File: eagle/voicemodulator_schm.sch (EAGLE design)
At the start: 39 parts, among them T1 2N5089, T2 2N5089, T3 2N5089, T4 2N5089

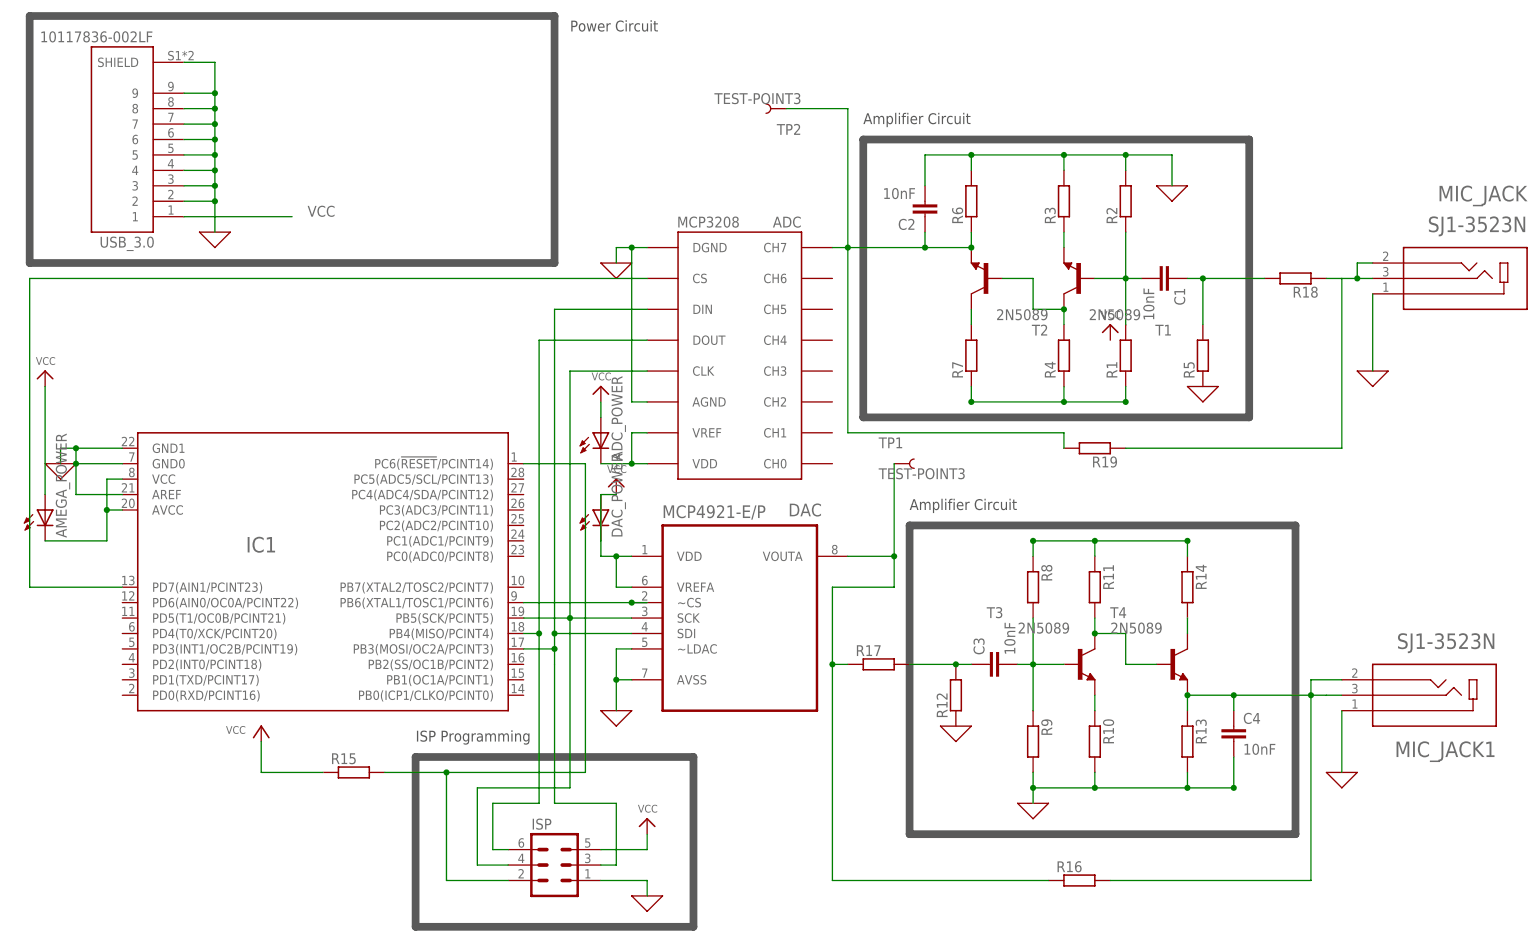
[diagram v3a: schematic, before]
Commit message: Grounded LEDs on power pins, added bypass caps at power pins
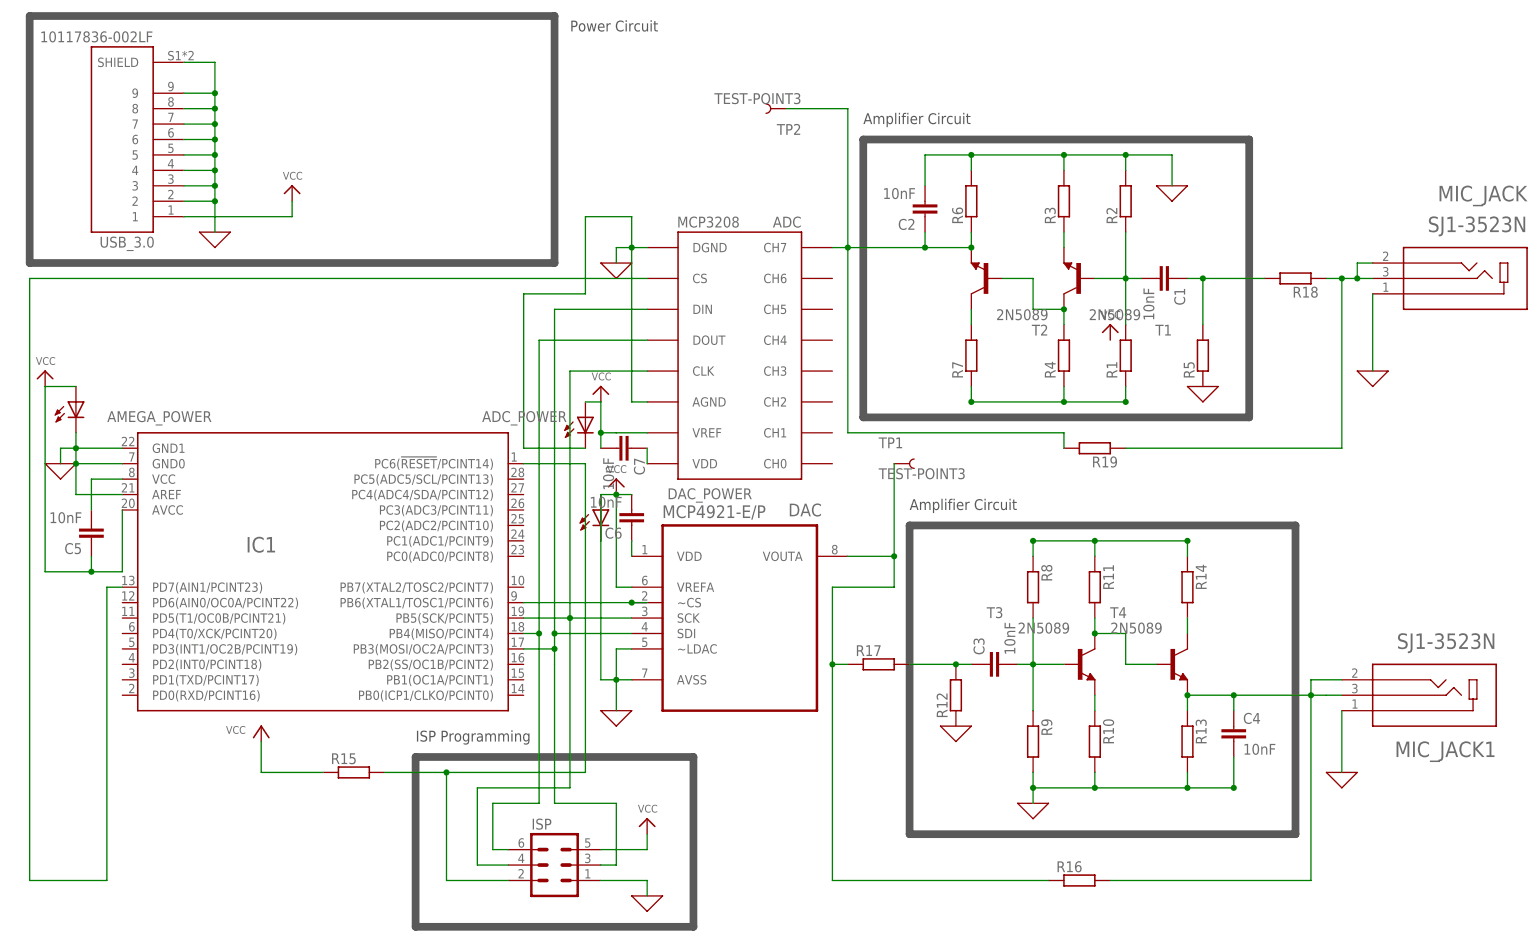
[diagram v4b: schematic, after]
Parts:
- added C5, C6, C7: 10nF, SparkFun-Capacitors:10NF-0603-50V-10%
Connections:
- removed net 0: ADC.AGND, ADC.DGND, C2.2, C4.2, DAC.AVSS, DAC.~LDAC, IC1.AREF, IC1.GND0, IC1.GND1, ISP.1, MIC_JACK.1, MIC_JACK1.1, R10.1, R12.2, R13.1, R2.1, R3.1, R5.2, R6.1, R9.1, USB_3.0.2, USB_3.0.3, USB_3.0.4, USB_3.0.5, USB_3.0.6, USB_3.0.7, USB_3.0.8, USB_3.0.9, USB_3.0.SHIELD
- new net GND: ADC.AGND, ADC.DGND, ADC_POWER.C, AMEGA_POWER.C, C2.2, C4.2, C6.2, DAC.AVSS, DAC.VREFA, DAC.~LDAC, DAC_POWER.A, DAC_POWER.C, IC1.AREF, IC1.GND0, IC1.GND1, ISP.1, MIC_JACK.1, MIC_JACK1.1, R10.1, R12.2, R13.1, R2.1, R3.1, R5.2, R6.1, R9.1, USB_3.0.2, USB_3.0.3, USB_3.0.4, USB_3.0.5, USB_3.0.6, USB_3.0.7, USB_3.0.8, USB_3.0.9, USB_3.0.SHIELD
- new net N$25: C5.2, IC1.VCC
- net N$18: now also C6.1, DAC.VDD; no longer ADC.VDD, ADC.VREF, ADC_POWER.C
- net N$21: now also ADC.VDD, C7.1; no longer AMEGA_POWER.C, IC1.AVCC, IC1.VCC
- net VCC: now also ADC.VREF, C5.1, C7.2, IC1.AVCC; no longer DAC.VDD, DAC.VREFA, DAC_POWER.A, DAC_POWER.C
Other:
- moved on the sheet: ADC_POWER, AMEGA_POWER

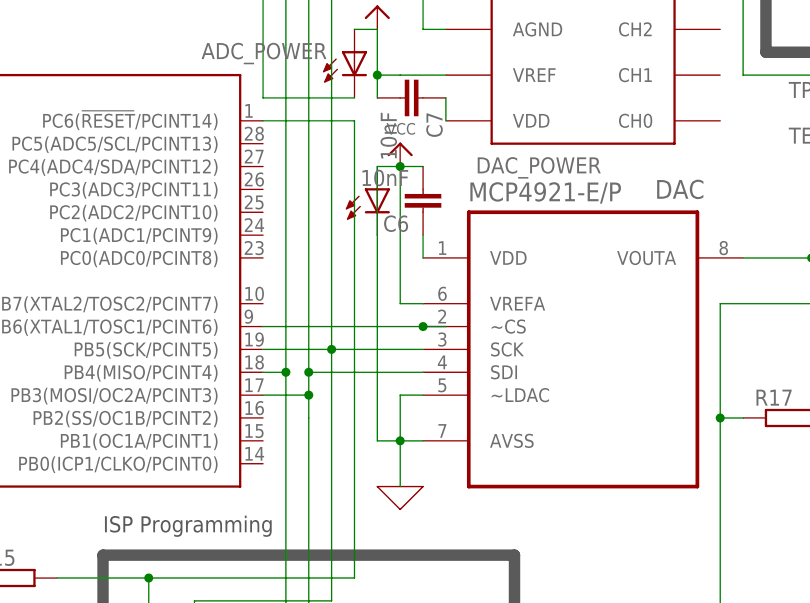
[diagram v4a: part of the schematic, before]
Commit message: Fixed erc error I missed on DAC
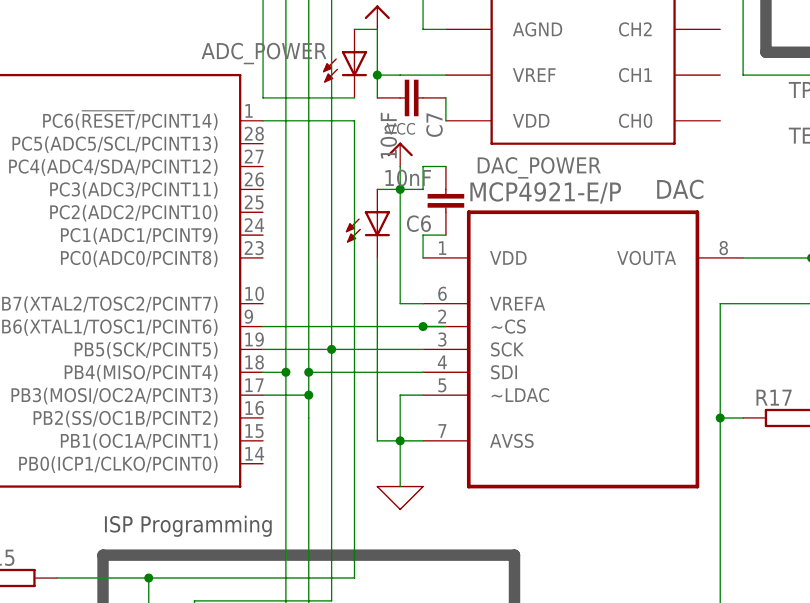
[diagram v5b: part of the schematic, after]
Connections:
- net GND: no longer C6.2, DAC.VREFA, DAC_POWER.A
- net VCC: now also C6.2, DAC.VREFA, DAC_POWER.A
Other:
- moved on the sheet: C6, DAC_POWER
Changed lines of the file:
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@@
 <attribute name="VALUE" x="48.895" y="46.228" size="1.778" layer="96" rot="R90"/>
 </instance>
-<instance part="DAC_POWER" gate="G$1" x="45.72" y="35.56">
+<instance part="DAC_POWER" gate="G$1" x="45.72" y="33.02">
 <attribute name="NAME" x="70.612" y="39.116" size="1.778" layer="95" rot="R180"/>
-<attribute name="VALUE" x="51.435" y="30.988" size="1.778" layer="96" rot="R90"/>
+<attribute name="VALUE" x="51.435" y="28.448" size="1.778" layer="96" rot="R90"/>
 </instance>
 <instance part="AMEGA_POWER" gate="G$1" x="-40.64" y="53.34">
@@
 <attribute name="VALUE" x="-39.624" y="35.179" size="1.778" layer="96" font="vector" rot="R180"/>
 </instance>
-<instance part="C6" gate="G$1" x="50.8" y="35.56" rot="R180">
-<attribute name="NAME" x="49.276" y="32.639" size="1.778" layer="95" font="vector" rot="R180"/>
-<attribute name="VALUE" x="49.276" y="37.719" size="1.778" layer="96" font="vector" rot="R180"/>
+<instance part="C6" gate="G$1" x="53.34" y="35.56" rot="R180">
+<attribute name="NAME" x="51.816" y="32.639" size="1.778" layer="95" font="vector" rot="R180"/>
+<attribute name="VALUE" x="51.816" y="37.719" size="1.778" layer="96" font="vector" rot="R180"/>
 </instance>
 <instance part="C7" gate="G$1" x="48.26" y="45.72" rot="R270">
@@
 <wire x1="50.8" y1="7.62" x2="48.26" y2="7.62" width="0.1524" layer="91"/>
 <junction x="48.26" y="7.62"/>
-<pinref part="P+1" gate="VCC" pin="VCC"/>
-<pinref part="DAC_POWER" gate="G$1" pin="A"/>
-<wire x1="48.26" y1="38.1" x2="45.72" y2="38.1" width="0.1524" layer="91"/>
 <pinref part="DAC_POWER" gate="G$1" pin="C"/>
-<wire x1="45.72" y1="38.1" x2="45.72" y2="30.48" width="0.1524" layer="91"/>
-<pinref part="DAC" gate="A" pin="VREFA"/>
-<wire x1="50.8" y1="22.86" x2="48.26" y2="22.86" width="0.1524" layer="91"/>
-<wire x1="48.26" y1="22.86" x2="48.26" y2="38.1" width="0.1524" layer="91"/>
-<junction x="48.26" y="38.1"/>
-<wire x1="45.72" y1="30.48" x2="45.72" y2="7.62" width="0.1524" layer="91"/>
+<wire x1="45.72" y1="27.94" x2="45.72" y2="7.62" width="0.1524" layer="91"/>
 <wire x1="48.26" y1="7.62" x2="45.72" y2="7.62" width="0.1524" layer="91"/>
-<wire x1="50.8" y1="38.1" x2="48.26" y2="38.1" width="0.1524" layer="91"/>
-<pinref part="C6" gate="G$1" pin="2"/>
 </segment>
 <segment>
@@
 <wire x1="-5.08" y1="83.82" x2="-5.08" y2="86.36" width="0.1524" layer="91"/>
 </segment>
+<segment>
+<pinref part="DAC_POWER" gate="G$1" pin="A"/>
+<pinref part="P+1" gate="VCC" pin="VCC"/>
+<pinref part="DAC" gate="A" pin="VREFA"/>
+<wire x1="50.8" y1="22.86" x2="48.26" y2="22.86" width="0.1524" layer="91"/>
+<wire x1="48.26" y1="22.86" x2="48.26" y2="35.56" width="0.1524" layer="91"/>
+<pinref part="C6" gate="G$1" pin="2"/>
+<wire x1="48.26" y1="35.56" x2="48.26" y2="38.1" width="0.1524" layer="91"/>
+<wire x1="53.34" y1="38.1" x2="50.8" y2="38.1" width="0.1524" layer="91"/>
+<wire x1="50.8" y1="38.1" x2="50.8" y2="35.56" width="0.1524" layer="91"/>
+<wire x1="50.8" y1="35.56" x2="48.26" y2="35.56" width="0.1524" layer="91"/>
+<wire x1="48.26" y1="35.56" x2="45.72" y2="35.56" width="0.1524" layer="91"/>
+<junction x="48.26" y="35.56"/>
+</segment>
 </net>
 <net name="N$2" class="0">
@@
 <pinref part="DAC" gate="A" pin="VDD"/>
 <pinref part="C6" gate="G$1" pin="1"/>
-<wire x1="50.8" y1="27.94" x2="50.8" y2="30.48" width="0.1524" layer="91"/>
-</segment>
-</net>
+<wire x1="53.34" y1="30.48" x2="50.8" y2="30.48" width="0.1524" layer="91"/>
+<wire x1="50.8" y1="30.48" x2="50.8" y2="27.94" width="0.1524" layer="91"/>
+</segment>
+</net>

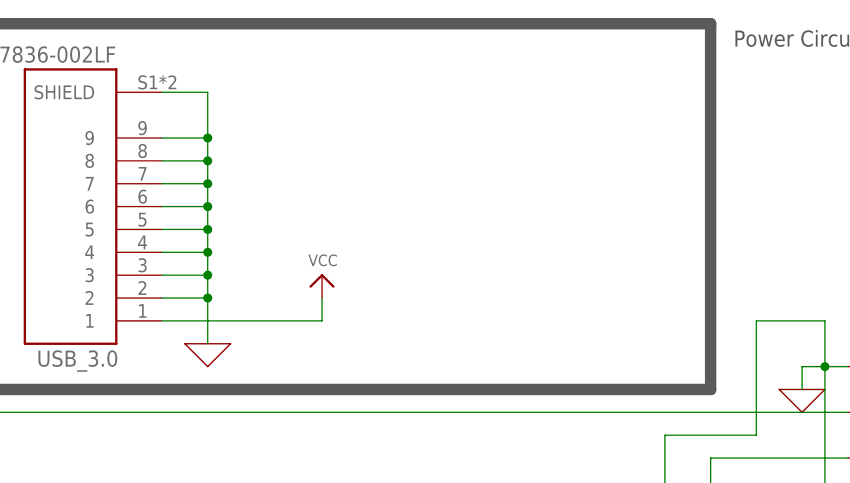
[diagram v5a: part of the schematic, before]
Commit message: Add caps for input voltage coming in through USB 3.0, remaining wire widths resolved.
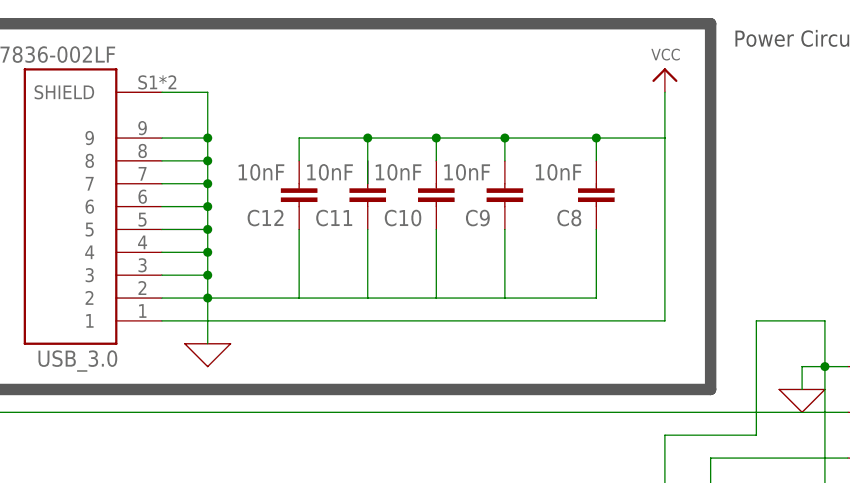
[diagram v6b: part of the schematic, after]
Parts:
- added C10, C11, C12, C8, C9: 10nF, SparkFun-Capacitors:10NF-0603-50V-10%
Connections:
- net GND: now also C10.1, C11.1, C12.1, C8.1, C9.1
- net VCC: now also C10.2, C12.2, C8.2, C9.2
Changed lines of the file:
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@@
 <part name="C6" library="SparkFun-Capacitors" library_urn="urn:adsk.eagle:library:510" deviceset="10NF" device="-0603-50V-10%" package3d_urn="urn:adsk.eagle:package:37414/1" value="10nF"/>
 <part name="C7" library="SparkFun-Capacitors" library_urn="urn:adsk.eagle:library:510" deviceset="10NF" device="-0603-50V-10%" package3d_urn="urn:adsk.eagle:package:37414/1" value="10nF"/>
+<part name="C8" library="SparkFun-Capacitors" library_urn="urn:adsk.eagle:library:510" deviceset="10NF" device="-0603-50V-10%" package3d_urn="urn:adsk.eagle:package:37414/1" value="10nF"/>
+<part name="C9" library="SparkFun-Capacitors" library_urn="urn:adsk.eagle:library:510" deviceset="10NF" device="-0603-50V-10%" package3d_urn="urn:adsk.eagle:package:37414/1" value="10nF"/>
+<part name="C10" library="SparkFun-Capacitors" library_urn="urn:adsk.eagle:library:510" deviceset="10NF" device="-0603-50V-10%" package3d_urn="urn:adsk.eagle:package:37414/1" value="10nF"/>
+<part name="C11" library="SparkFun-Capacitors" library_urn="urn:adsk.eagle:library:510" deviceset="10NF" device="-0603-50V-10%" package3d_urn="urn:adsk.eagle:package:37414/1" value="10nF"/>
+<part name="C12" library="SparkFun-Capacitors" library_urn="urn:adsk.eagle:library:510" deviceset="10NF" device="-0603-50V-10%" package3d_urn="urn:adsk.eagle:package:37414/1" value="10nF"/>
 </parts>
 <sheets>
@@
 </instance>
 <instance part="X_11" gate="G$1" x="-17.78" y="81.28"/>
-<instance part="P+7" gate="VCC" x="-5.08" y="88.9">
-<attribute name="VALUE" x="-6.604" y="89.916" size="1.27" layer="96"/>
+<instance part="P+7" gate="VCC" x="33.02" y="111.76">
+<attribute name="VALUE" x="31.496" y="112.776" size="1.27" layer="96"/>
 </instance>
 <instance part="C5" gate="G$1" x="-38.1" y="33.02" rot="R180">
@@
 <attribute name="NAME" x="51.181" y="44.196" size="1.778" layer="95" font="vector" rot="R270"/>
 <attribute name="VALUE" x="46.101" y="44.196" size="1.778" layer="96" font="vector" rot="R270"/>
+</instance>
+<instance part="C8" gate="G$1" x="25.4" y="99.06" rot="R180">
+<attribute name="NAME" x="23.876" y="96.139" size="1.778" layer="95" font="vector" rot="R180"/>
+<attribute name="VALUE" x="23.876" y="101.219" size="1.778" layer="96" font="vector" rot="R180"/>
+</instance>
+<instance part="C9" gate="G$1" x="15.24" y="99.06" rot="R180">
+<attribute name="NAME" x="13.716" y="96.139" size="1.778" layer="95" font="vector" rot="R180"/>
+<attribute name="VALUE" x="13.716" y="101.219" size="1.778" layer="96" font="vector" rot="R180"/>
+</instance>
+<instance part="C10" gate="G$1" x="7.62" y="99.06" rot="R180">
+<attribute name="NAME" x="6.096" y="96.139" size="1.778" layer="95" font="vector" rot="R180"/>
+<attribute name="VALUE" x="6.096" y="101.219" size="1.778" layer="96" font="vector" rot="R180"/>
+</instance>
+<instance part="C11" gate="G$1" x="0" y="99.06" rot="R180">
+<attribute name="NAME" x="-1.524" y="96.139" size="1.778" layer="95" font="vector" rot="R180"/>
+<attribute name="VALUE" x="-1.524" y="101.219" size="1.778" layer="96" font="vector" rot="R180"/>
+</instance>
+<instance part="C12" gate="G$1" x="-7.62" y="99.06" rot="R180">
+<attribute name="NAME" x="-9.144" y="96.139" size="1.778" layer="95" font="vector" rot="R180"/>
+<attribute name="VALUE" x="-9.144" y="101.219" size="1.778" layer="96" font="vector" rot="R180"/>
 </instance>
 </instances>
@@
 <wire x1="-17.78" y1="109.22" x2="-17.78" y2="104.14" width="0.1524" layer="91"/>
 <junction x="-17.78" y="104.14"/>
+<pinref part="C8" gate="G$1" pin="1"/>
+<wire x1="-17.78" y1="86.36" x2="-7.62" y2="86.36" width="0.1524" layer="91"/>
+<wire x1="-7.62" y1="86.36" x2="0" y2="86.36" width="0.1524" layer="91"/>
+<wire x1="7.62" y1="86.36" x2="15.24" y2="86.36" width="0.1524" layer="91"/>
+<wire x1="15.24" y1="86.36" x2="25.4" y2="86.36" width="0.1524" layer="91"/>
+<wire x1="25.4" y1="86.36" x2="25.4" y2="93.98" width="0.1524" layer="91"/>
+<pinref part="C9" gate="G$1" pin="1"/>
+<wire x1="15.24" y1="86.36" x2="15.24" y2="93.98" width="0.1524" layer="91"/>
+<pinref part="C10" gate="G$1" pin="1"/>
+<wire x1="7.62" y1="93.98" x2="7.62" y2="86.36" width="0.1524" layer="91"/>
+<pinref part="C11" gate="G$1" pin="1"/>
+<wire x1="7.62" y1="86.36" x2="0" y2="86.36" width="0.1524" layer="91"/>
+<wire x1="0" y1="86.36" x2="0" y2="93.98" width="0.1524" layer="91"/>
+<pinref part="C12" gate="G$1" pin="1"/>
+<wire x1="-7.62" y1="86.36" x2="-7.62" y2="93.98" width="0.1524" layer="91"/>
 </segment>
 </net>
@@
 <segment>
 <pinref part="USB_3.0" gate="G$1" pin="1"/>
-<wire x1="-22.86" y1="83.82" x2="-5.08" y2="83.82" width="0.1524" layer="91"/>
+<wire x1="-22.86" y1="83.82" x2="33.02" y2="83.82" width="0.1524" layer="91"/>
 <pinref part="P+7" gate="VCC" pin="VCC"/>
-<wire x1="-5.08" y1="83.82" x2="-5.08" y2="86.36" width="0.1524" layer="91"/>
-</segment>
-<segment>
+<wire x1="33.02" y1="83.82" x2="33.02" y2="104.14" width="0.1524" layer="91"/>
+<pinref part="C12" gate="G$1" pin="2"/>
+<wire x1="33.02" y1="104.14" x2="33.02" y2="109.22" width="0.1524" layer="91"/>
+<wire x1="-7.62" y1="101.6" x2="-7.62" y2="104.14" width="0.1524" layer="91"/>
+<wire x1="-7.62" y1="104.14" x2="0" y2="104.14" width="0.1524" layer="91"/>
+<wire x1="0" y1="104.14" x2="7.62" y2="104.14" width="0.1524" layer="91"/>
+<wire x1="15.24" y1="104.14" x2="25.4" y2="104.14" width="0.1524" layer="91"/>
+<wire x1="33.02" y1="104.14" x2="25.4" y2="104.14" width="0.1524" layer="91"/>
+<pinref part="C8" gate="G$1" pin="2"/>
+<wire x1="25.4" y1="104.14" x2="25.4" y2="101.6" width="0.1524" layer="91"/>
+<pinref part="C9" gate="G$1" pin="2"/>
+<wire x1="15.24" y1="101.6" x2="15.24" y2="104.14" width="0.1524" layer="91"/>
+<pinref part="C10" gate="G$1" pin="2"/>
+<wire x1="15.24" y1="104.14" x2="7.62" y2="104.14" width="0.1524" layer="91"/>
+<wire x1="7.62" y1="104.14" x2="7.62" y2="101.6" width="0.1524" layer="91"/>
+<wire x1="0" y1="104.14" x2="0" y2="99.06" width="0.1524" layer="91"/>
+<junction x="0" y="104.14"/>
+<junction x="7.62" y="104.14"/>
+<junction x="15.24" y="104.14"/>
+<junction x="25.4" y="104.14"/>
+</segment>
+<segment>
